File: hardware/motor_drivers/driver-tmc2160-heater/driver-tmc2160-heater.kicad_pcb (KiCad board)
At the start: 4 copper layers, 30 x 31 mm, 79 parts, among them J1 XH, J2 MF3 1x2P, Q1 DMT6016, Q2 DMT6016, Q3 DMT6016, Q4 DMT6016, Q5 DMT6016, Q6 DMT6016, Q7 DMT6016, Q8 DMT6016, Q9 NMOS, T10 CS0, T11 STEP, T12 GND, T13 DIR, T14 EN, T15 HEAT, T16 GND, T17 DIAG, T3 12V, T4 SCK, T5 GND, T6 SDI, T7 SDO, T8 VCC, T9 Therm, U1 TMC2160, U2 UCC27517

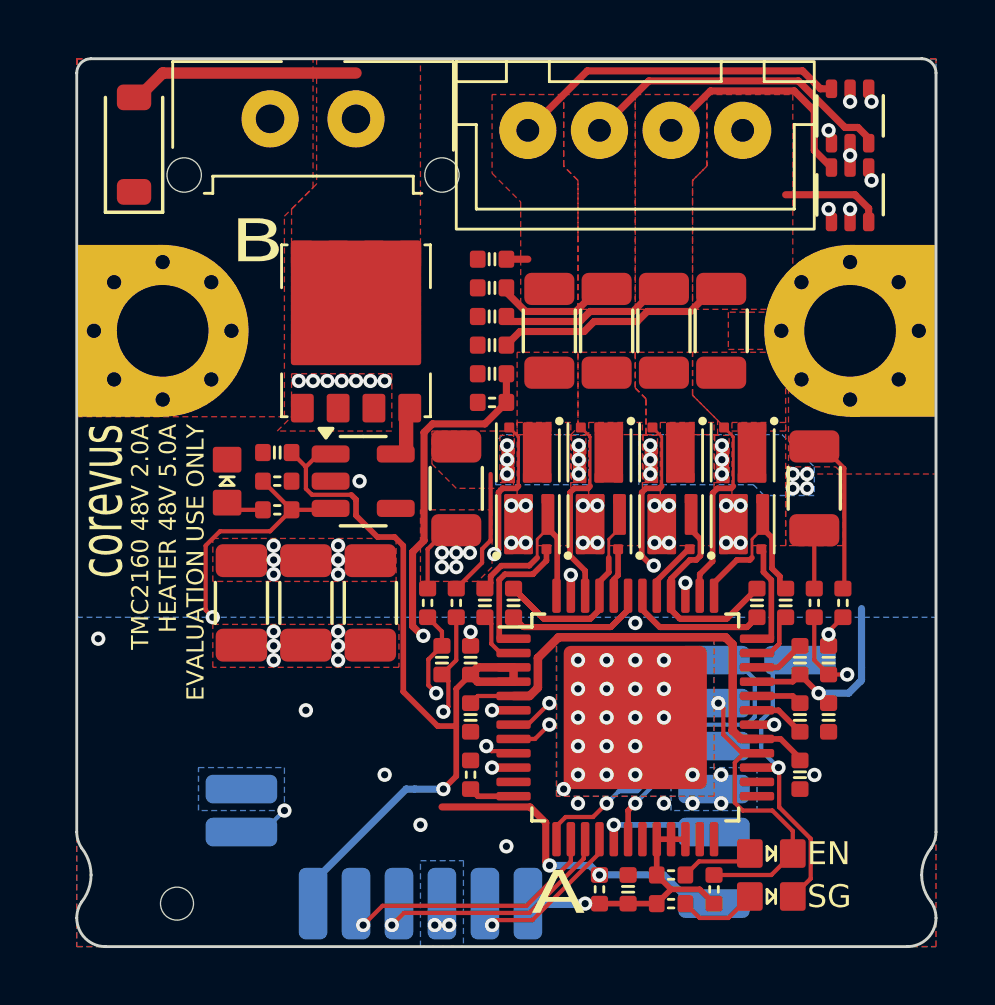
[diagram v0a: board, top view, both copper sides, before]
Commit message: Added STEP and Parasolid mechanical files for Corevus-G v0.6, added TMC2160 + Heater module, added toolboard 4x thermistor expansion, added toolboard MAX31856 thermocouple ADC expansion
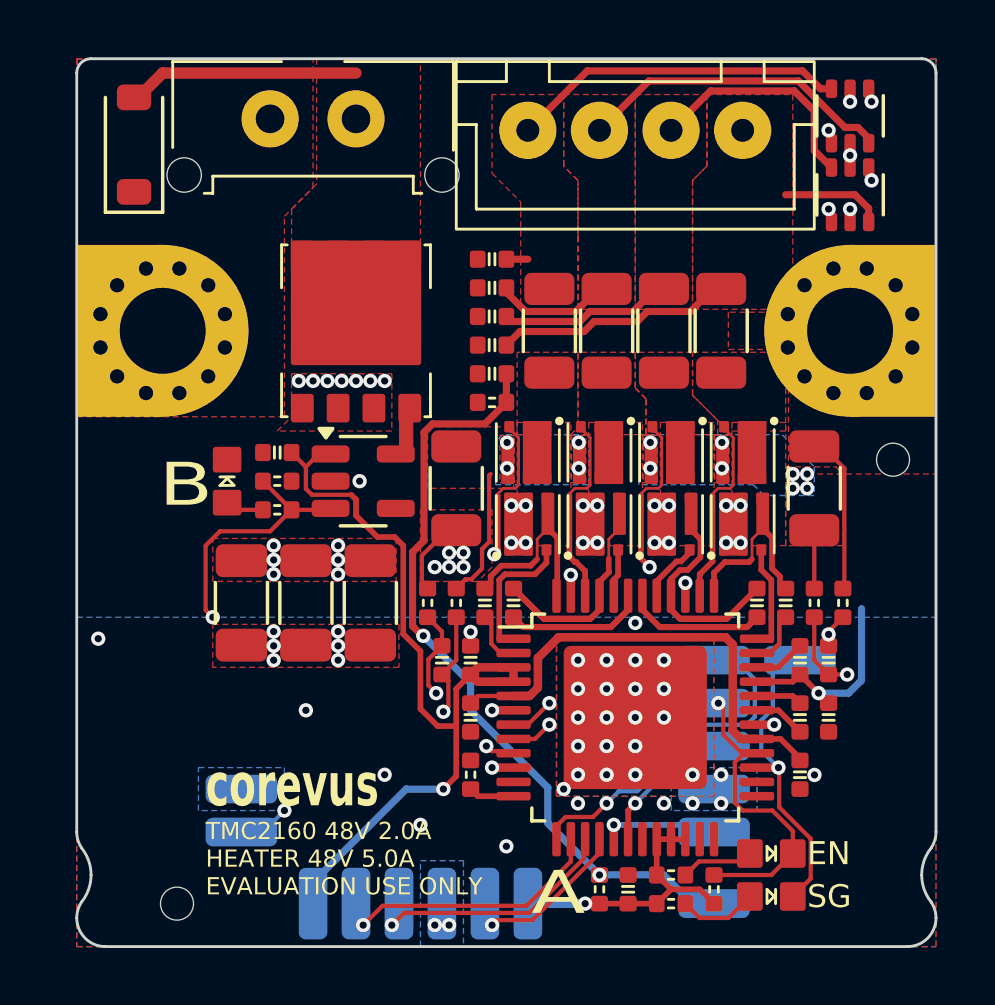
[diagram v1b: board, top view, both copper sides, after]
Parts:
- added H3: ToolingHole, corevus:ToolingHole, F.Cu at (148.5, 64.5)
- R10, R13: value 50mΩ -> 100mΩ
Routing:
- net /THERM: track 24.2 -> 27.8 mm, vias 3 -> 2
- net Net-(Q2-S-Pad4): track 4.50 -> 4.61 mm, vias 6 -> 4
- net Net-(Q6-S-Pad4): vias 10 -> 8

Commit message: update toolboard, change documentation
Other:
- board text added: "MERIDI ENGINEERING SEP 2024 HEATER + TMC2160 DRIVER MODULE TMC2160: 48V 2.0A(rms) MAX HEATER: 48V 5.0A MAX"
- board text added: "TMC2160 48V 2.0A HEATER 48V 5.0A"
- board text removed: "NOT FOR PRODUCTION USE MERIDI ENGINEERING JULY 2024 TMC2160 EXTRUDER HEATER COMBO TMC2160: 48V 2.0A(rms) MAX HEATER: 48V 5.0A MAX"
- board text removed: "TMC2160 48V 2.0A HEATER 48V 5.0A EVALUATION USE ONLY"
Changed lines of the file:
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@@
 	)
 	(gr_text "A"
-		(at 143.75 72.750001 0)
+		(at 143.75 72.5 0)
 		(layer "B.SilkS" knockout)
 		(effects
@@
 		)
 	)
-	(gr_text "NOT FOR PRODUCTION USE\nMERIDI ENGINEERING JULY 2024\nTMC2160 EXTRUDER HEATER COMBO\nTMC2160: 48V 2.0A(rms) MAX\nHEATER: 48V 5.0A MAX"
-		(at 135 57 0)
+	(gr_text "MERIDI ENGINEERING SEP 2024\nHEATER + TMC2160 DRIVER MODULE\nTMC2160: 48V 2.0A(rms) MAX\nHEATER: 48V 5.0A MAX"
+		(at 135 57.5 0)
 		(layer "B.SilkS")
 		(effects
@@
 	)
 	(gr_text "corevus"
-		(at 124.5 76.75 0)
+		(at 124.5 80.75 0)
 		(layer "F.SilkS")
 		(effects
@@
 		)
 	)
-	(gr_text "TMC2160 48V 2.0A\nHEATER 48V 5.0A\nEVALUATION USE ONLY"
-		(at 124.5 79.75 0)
+	(gr_text "TMC2160 48V 2.0A\nHEATER 48V 5.0A"
+		(at 149.5 65.75 90)
 		(layer "F.SilkS")
 		(effects
@@
 				(thickness 0.15)
 			)
-			(justify left bottom)
+			(justify right bottom)
 		)
 	)
@@
 	)
 	(zone
+		(net 12)
+		(net_name "+48V")
+		(layer "B.Cu")
+		(hatch edge 0.5)
+		(priority 4)
+		(connect_pads
+			(clearance 0.15)
+		)
+		(min_thickness 0.25)
+		(filled_areas_thickness no)
+		(fill yes
+			(thermal_gap 0.25)
+			(thermal_bridge_width 1)
+		)
+		(polygon
+			(pts
+				(xy 120 50.5) (xy 120 54.5) (xy 150 54.5) (xy 150 50.5)
+			)
+		)
+	)
+	(zone
 		(net 34)
 		(net_name "Net-(Q2-S-Pad4)")
@@
 		(polygon
 			(pts
-				(xy 120 50.5) (xy 120 70) (xy 150 70) (xy 150 50.5)
+				(xy 120 54.5) (xy 120 70) (xy 150 70) (xy 150 54.5)
 			)
 		)
